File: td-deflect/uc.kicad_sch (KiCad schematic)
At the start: 18 parts, among them J4 Conn_ARM_JTAG_SWD_10, J6 Conn_01x06_Male, U12 LM1117-5.0, U2 STM32G474xx, U3 INA193, U4 TPS70933, X1 SG-8002CA

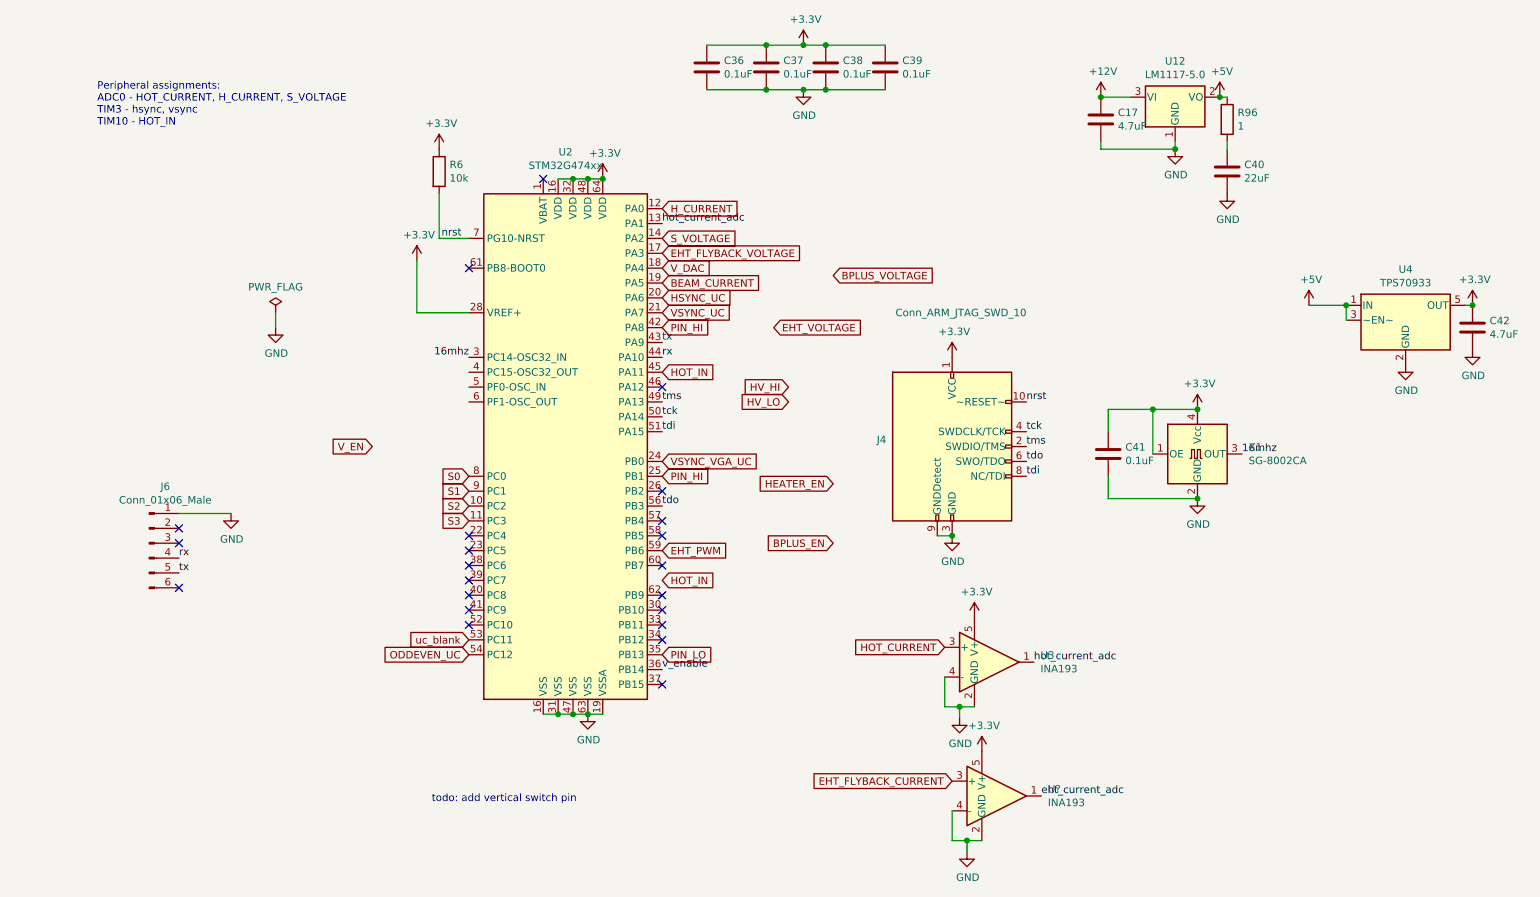
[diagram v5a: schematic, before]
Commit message: add connector for power
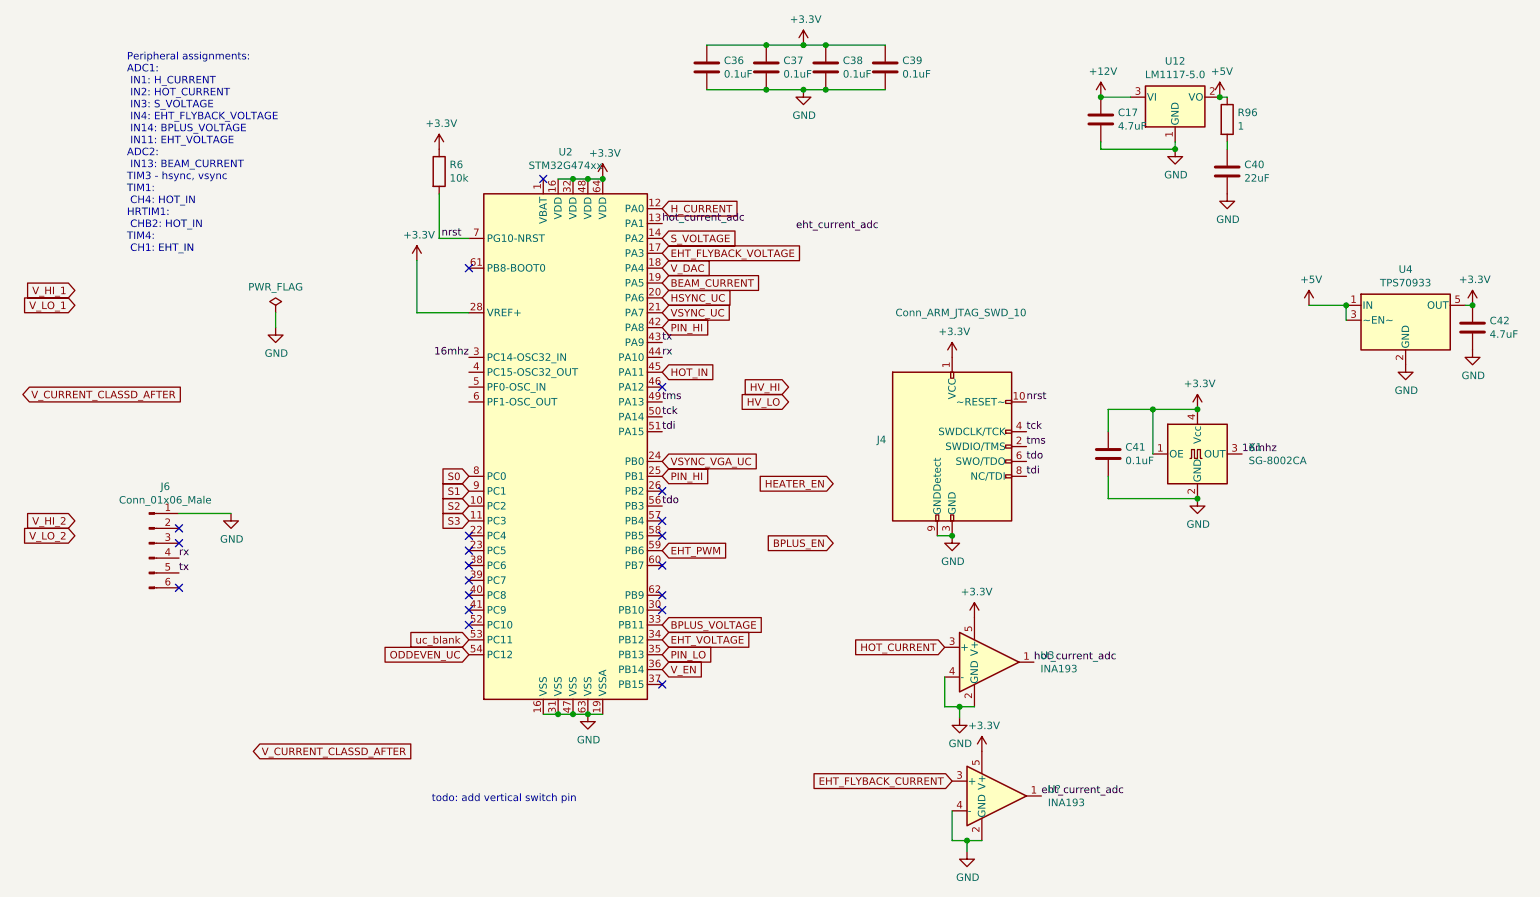
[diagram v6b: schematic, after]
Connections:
- net v_enable is gone; now on net V_EN: U2.36 (PB14)
- net BPLUS_VOLTAGE: now also U2.33 (PB11)
- net EHT_VOLTAGE: now also U2.34 (PB12)
- no-connect marks 22 -> 20
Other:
- note added: "Peripheral assignments: ADC1: IN1: H_CURRENT IN2: HOT_CURRENT IN3: S_VOLTAGE IN4: EHT_FLYBACK_VOLTAGE IN14: BPLUS_VOLTAGE IN11: EHT_VOLTAGE ADC2: IN13: BEAM_CURRENT TIM3 - hsync, vsync TIM1: CH4: HOT_IN HRTIM1: CHB2: HOT_IN TIM4: CH1: EHT_IN"
- note removed: "Peripheral assignments: ADC0 - HOT_CURRENT, H_CURRENT, S_VOLTAGE TIM3 - hsync, vsync TIM10 - HOT_IN"
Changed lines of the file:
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@@
   (no_connect (at 50.8 106.68))
   (no_connect (at 133.35 102.87))
-  (no_connect (at 133.35 123.19))
   (no_connect (at 100.33 107.95))
   (no_connect (at 100.33 113.03))
@@
   (no_connect (at 100.33 118.11))
   (no_connect (at 100.33 105.41))
-  (no_connect (at 133.35 120.65))
   (wire (pts (xy 208.28 39.37) (xy 220.98 39.37))
     (stroke (width 0) (type solid) (color 0 0 0 0))
@@
     (stroke (width 0) (type default) (color 0 0 0 0))
   )
-  (text "Peripheral assignments:\nADC0 - HOT_CURRENT, H_CURRENT, S_VOLTAGE\nTIM3 - hsync, vsync\nTIM10 - HOT_IN"
-    (at 36.83 35.56 0)
+  (text "Peripheral assignments:\nADC1:\n IN1: H_CURRENT\n IN2: HOT_CURRENT\n IN3: S_VOLTAGE\n IN4: EHT_FLYBACK_VOLTAGE\n IN14: BPLUS_VOLTAGE\n IN11: EHT_VOLTAGE\nADC2:\n IN13: BEAM_CURRENT\nTIM3 - hsync, vsync\nTIM1:\n CH4: HOT_IN\nHRTIM1:\n CHB2: HOT_IN\nTIM4:\n CH1: EHT_IN"
+    (at 41.91 57.15 0)
     (effects (font (size 1.27 1.27)) (justify left bottom))
   )
@@
     (effects (font (size 1.27 1.27)) (justify left bottom))
   )
-  (label "v_enable" (at 133.35 128.27 0)
-    (effects (font (size 1.27 1.27)) (justify left bottom))
-  )
   (label "nrst" (at 195.58 82.55 0)
     (effects (font (size 1.27 1.27)) (justify left bottom))
@@
   )
   (label "tx" (at 133.35 72.39 0)
+    (effects (font (size 1.27 1.27)) (justify left bottom))
+  )
+  (label "eht_current_adc" (at 156.21 53.34 0)
     (effects (font (size 1.27 1.27)) (justify left bottom))
   )
@@
     )
   )
+  (global_label "V_CURRENT_CLASSD_AFTER" (shape input) (at 24.13 81.28 0) (fields_autoplaced)
+    (effects (font (size 1.27 1.27)) (justify left))
+    (property "Intersheet References" "${INTERSHEET_REFS}" (id 0) (at 51.6728 81.2006 0)
+      (effects (font (size 1.27 1.27)) (justify left) hide)
+    )
+  )
+  (global_label "V_LO_1" (shape input) (at 33.02 66.04 180) (fields_autoplaced)
+    (effects (font (size 1.27 1.27)) (justify right))
+    (property "Intersheet References" "${INTERSHEET_REFS}" (id 0) (at 24.1039 65.9606 0)
+      (effects (font (size 1.27 1.27)) (justify right) hide)
+    )
+  )
   (global_label "HV_HI" (shape input) (at 154.94 80.01 180) (fields_autoplaced)
     (effects (font (size 1.27 1.27)) (justify right))
@@
     )
   )
+  (global_label "V_HI_1" (shape input) (at 33.02 63.5 180) (fields_autoplaced)
+    (effects (font (size 1.27 1.27)) (justify right))
+    (property "Intersheet References" "${INTERSHEET_REFS}" (id 0) (at 24.5272 63.4206 0)
+      (effects (font (size 1.27 1.27)) (justify right) hide)
+    )
+  )
   (global_label "BEAM_CURRENT" (shape input) (at 133.35 62.23 0) (fields_autoplaced)
     (effects (font (size 1.27 1.27)) (justify left))
@@
     )
   )
+  (global_label "V_HI_2" (shape input) (at 33.02 102.87 180) (fields_autoplaced)
+    (effects (font (size 1.27 1.27)) (justify right))
+    (property "Intersheet References" "${INTERSHEET_REFS}" (id 0) (at 24.5272 102.7906 0)
+      (effects (font (size 1.27 1.27)) (justify right) hide)
+    )
+  )
   (global_label "HEATER_EN" (shape input) (at 162.56 96.52 180) (fields_autoplaced)
     (effects (font (size 1.27 1.27)) (justify right))
@@
     )
   )
+  (global_label "V_CURRENT_CLASSD_AFTER" (shape input) (at 63.5 142.24 0) (fields_autoplaced)
+    (effects (font (size 1.27 1.27)) (justify left))
+    (property "Intersheet References" "${INTERSHEET_REFS}" (id 0) (at 91.0428 142.1606 0)
+      (effects (font (size 1.27 1.27)) (justify left) hide)
+    )
+  )
   (global_label "EHT_PWM" (shape input) (at 133.35 107.95 0) (fields_autoplaced)
     (effects (font (size 1.27 1.27)) (justify left))
@@
     )
   )
-  (global_label "V_EN" (shape input) (at 83.82 90.17 180) (fields_autoplaced)
-    (effects (font (size 1.27 1.27)) (justify right))
-    (property "Intersheet References" "${INTERSHEET_REFS}" (id 0) (at 76.9601 90.2494 0)
-      (effects (font (size 1.27 1.27)) (justify right) hide)
+  (global_label "V_EN" (shape input) (at 133.35 128.27 0) (fields_autoplaced)
+    (effects (font (size 1.27 1.27)) (justify left))
+    (property "Intersheet References" "${INTERSHEET_REFS}" (id 0) (at 140.2099 128.1906 0)
+      (effects (font (size 1.27 1.27)) (justify left) hide)
     )
   )
@@
     )
   )
+  (global_label "V_LO_2" (shape input) (at 33.02 105.41 180) (fields_autoplaced)
+    (effects (font (size 1.27 1.27)) (justify right))
+    (property "Intersheet References" "${INTERSHEET_REFS}" (id 0) (at 24.1039 105.3306 0)
+      (effects (font (size 1.27 1.27)) (justify right) hide)
+    )
+  )
   (global_label "S1" (shape input) (at 100.33 97.79 180) (fields_autoplaced)
     (effects (font (size 1.27 1.27)) (justify right))
@@
     )
   )
-  (global_label "BPLUS_VOLTAGE" (shape input) (at 162.56 60.96 0) (fields_autoplaced)
-    (effects (font (size 1.27 1.27)) (justify left))
-    (property "Intersheet References" "${INTERSHEET_REFS}" (id 0) (at 179.8823 60.8806 0)
-      (effects (font (size 1.27 1.27)) (justify left) hide)
-    )
-  )
-  (global_label "HOT_IN" (shape input) (at 133.35 113.03 0) (fields_autoplaced)
-    (effects (font (size 1.27 1.27)) (justify left))
-    (property "Intersheet References" "${INTERSHEET_REFS}" (id 0) (at 0 0 0)
-      (effects (font (size 1.27 1.27)) hide)
+  (global_label "BPLUS_VOLTAGE" (shape input) (at 133.35 120.65 0) (fields_autoplaced)
+    (effects (font (size 1.27 1.27)) (justify left))
+    (property "Intersheet References" "${INTERSHEET_REFS}" (id 0) (at 150.6723 120.5706 0)
+      (effects (font (size 1.27 1.27)) (justify left) hide)
     )
   )
@@
     )
   )
-  (global_label "EHT_VOLTAGE" (shape input) (at 152.4 69.85 0) (fields_autoplaced)
-    (effects (font (size 1.27 1.27)) (justify left))
-    (property "Intersheet References" "${INTERSHEET_REFS}" (id 0) (at 167.0613 69.7706 0)
-      (effects (font (size 1.27 1.27)) (justify left) hide)
-    )
+  (global_label "EHT_VOLTAGE" (shape input) (at 133.35 123.19 0) (fields_autoplaced)
+    (effects (font (size 1.27 1.27)) (justify left))
+    (property "Intersheet References" "${INTERSHEET_REFS}" (id 0) (at 148.0113 123.1106 0)
+      (effects (font (size 1.27 1.27)) (justify left) hide)
+    )

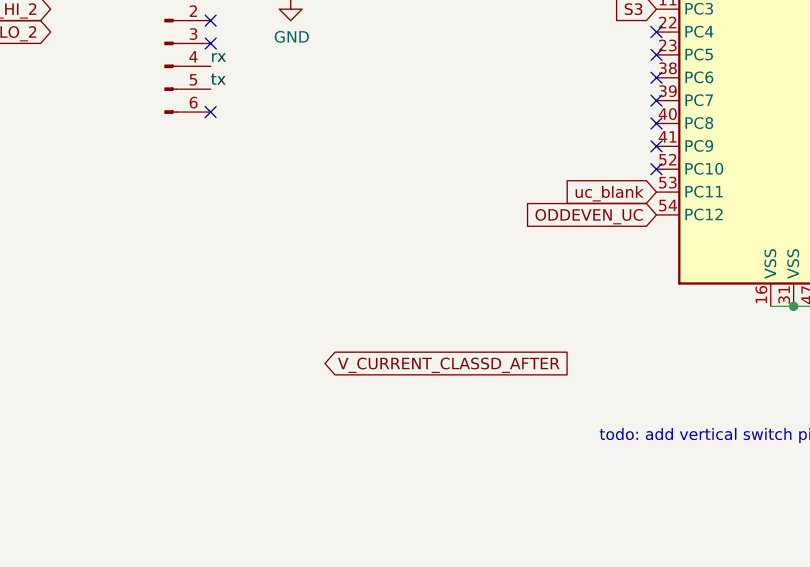
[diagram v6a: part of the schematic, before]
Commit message: add degauss circuit
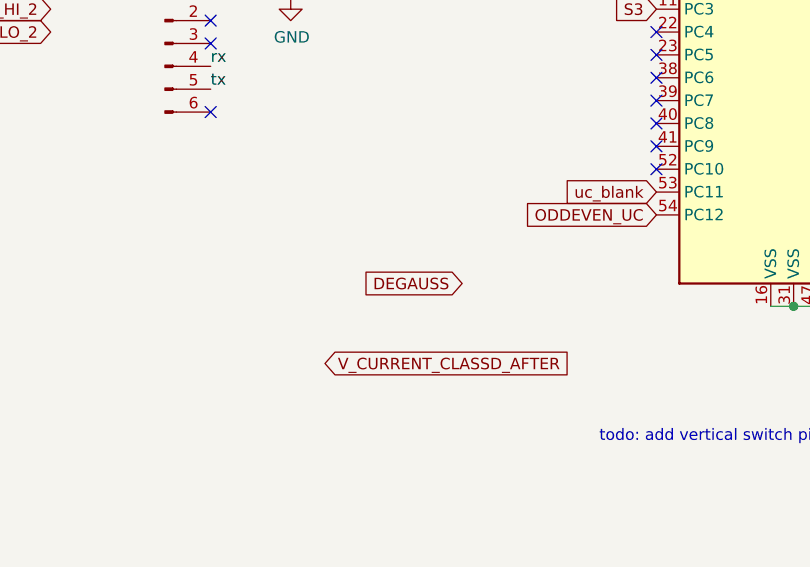
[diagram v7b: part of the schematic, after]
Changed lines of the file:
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@@
+    )
+  )
+  (global_label "DEGAUSS" (shape input) (at 78.74 133.35 180) (fields_autoplaced)
+    (effects (font (size 1.27 1.27)) (justify right))
+    (property "Intersheet References" "${INTERSHEET_REFS}" (id 0) (at 67.8887 133.4294 0)
+      (effects (font (size 1.27 1.27)) (justify right) hide)
     )
   )
